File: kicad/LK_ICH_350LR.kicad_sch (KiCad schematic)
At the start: 27 parts, among them Q1 BTA12-700SW, U2 PC123

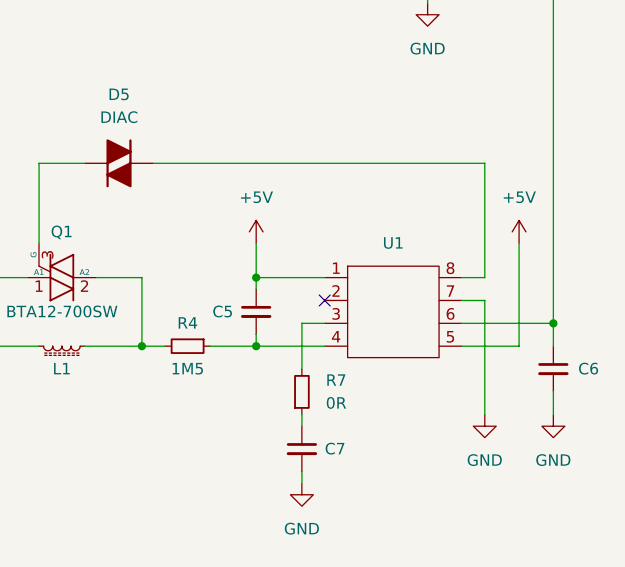
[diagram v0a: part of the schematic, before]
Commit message: update dimmer control ic symbol
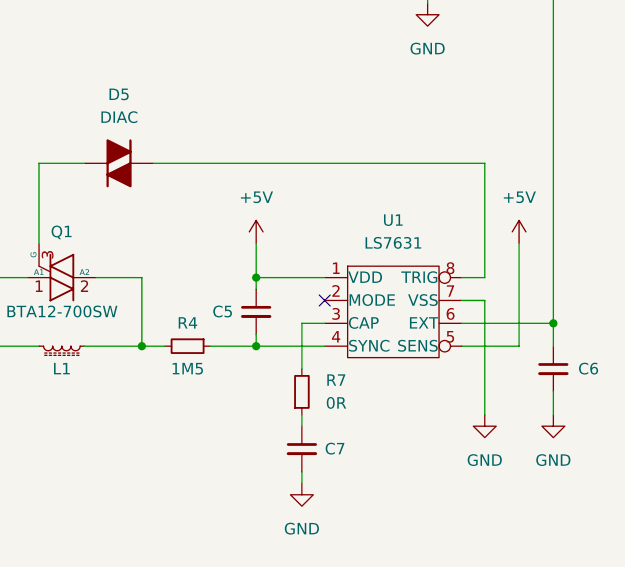
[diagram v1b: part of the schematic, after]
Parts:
- U1: value ~ -> LS7631; footprint (none) -> Package_SO:SOIC-8_3.9x4.9mm_P1.27mm; symbol LK913A4:DIM -> LK913A4:LS7631
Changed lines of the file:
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@@
     )
   )
-  (symbol (lib_id "LK913A4:DIM") (at 135.89 106.68 0) (unit 1)
+  (symbol (lib_id "LK913A4:LS7631") (at 135.89 106.68 0) (unit 1)
     (in_bom yes) (on_board yes) (dnp no) (fields_autoplaced)
-    (property "Reference" "U1" (at 135.89 99.06 0)
+    (property "Reference" "U1" (at 135.89 96.52 0)
       (effects (font (size 1.27 1.27)))
     )
-    (property "Value" "~" (at 135.89 106.68 0)
+    (property "Value" "LS7631" (at 135.89 99.06 0)
       (effects (font (size 1.27 1.27)))
     )
-    (property "Footprint" "" (at 135.89 106.68 0)
+    (property "Footprint" "Package_SO:SOIC-8_3.9x4.9mm_P1.27mm" (at 135.89 106.68 0)
       (effects (font (size 1.27 1.27)) hide)
     )
-    (property "Datasheet" "" (at 135.89 106.68 0)
+    (property "Datasheet" "http://www.lsicsi.com/pdfs/Data_Sheets/LS7631_LS7632.pdf" (at 135.89 106.68 0)
       (effects (font (size 1.27 1.27)) hide)
     )

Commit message: add note about diac
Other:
- note added: "This may not actually be a diac, but could be a small signal diode per the SLB0587 reference schematic."
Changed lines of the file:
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@@
   (title_block
     (title "LK ICH Dimmer 350 LR")
-    (date "2023-12-04")
-    (rev "1")
+    (date "2023-12-09")
+    (rev "2")
     (comment 1 "LK913CB4")
     (comment 2 "LK913A4")
@@
     (effects (font (size 1.27 1.27)) (justify left bottom))
   )
+  (text "This may not actually be a diac,\nbut could be a small signal diode\nper the SLB0587 reference schematic."
+    (at 64.77 86.36 0)
+    (effects (font (size 1.27 1.27)) (justify left bottom))
+  )

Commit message: fix capacitance of c3
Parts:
- C3: value 22u -> 100u
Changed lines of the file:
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@@
   (title_block
     (title "LK ICH Dimmer 350 LR")
-    (date "2023-12-09")
-    (rev "2")
+    (date "2023-12-17")
+    (rev "3")
     (comment 1 "LK913CB4")
     (comment 2 "LK913A4")
@@
       (effects (font (size 1.27 1.27)) (justify left))
     )
-    (property "Value" "22u" (at 128.27 171.45 0)
-      (effects (font (size 1.27 1.27)))
-    )
+    (property "Value" "100u" (at 128.27 171.45 0)
+      (effects (font (size 1.27 1.27)))
+    )

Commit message: fix annotations
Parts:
- renumbered C2 to C1, D3 to CR1, R5 to R2, R7 to R3, R1 to R5, R3 to R7, R2 to R8, D4 to VR1
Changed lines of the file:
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@@
   (symbol (lib_id "Device:R_Small") (at 153.67 68.58 180) (unit 1)
     (in_bom yes) (on_board yes) (dnp no) (fields_autoplaced)
-    (property "Reference" "R1" (at 156.21 67.31 0)
+    (property "Reference" "R5" (at 156.21 67.31 0)
       (effects (font (size 1.27 1.27)) (justify right))
     )
@@
       (project "LK_ICH_350LR"
         (path "/00661e67-d895-4a4d-8f6d-597ae5750c96"
-          (reference "R1") (unit 1)
+          (reference "R5") (unit 1)
         )
       )
@@
   (symbol (lib_id "Device:R_Small") (at 96.52 62.23 90) (mirror x) (unit 1)
     (in_bom yes) (on_board yes) (dnp no)
-    (property "Reference" "R3" (at 96.52 64.77 90)
+    (property "Reference" "R7" (at 96.52 64.77 90)
       (effects (font (size 1.27 1.27)))
     )
@@
       (project "LK_ICH_350LR"
         (path "/00661e67-d895-4a4d-8f6d-597ae5750c96"
-          (reference "R3") (unit 1)
+          (reference "R7") (unit 1)
         )
       )
@@
   (symbol (lib_id "Device:D_Zener_Small") (at 107.95 165.1 90) (mirror x) (unit 1)
     (in_bom yes) (on_board yes) (dnp no)
-    (property "Reference" "D4" (at 107.95 158.75 90)
+    (property "Reference" "VR1" (at 107.95 158.75 90)
       (effects (font (size 1.27 1.27)))
     )
@@
       (project "LK_ICH_350LR"
         (path "/00661e67-d895-4a4d-8f6d-597ae5750c96"
-          (reference "D4") (unit 1)
+          (reference "VR1") (unit 1)
         )
       )
@@
   (symbol (lib_id "Device:D_Small") (at 114.3 168.91 0) (mirror x) (unit 1)
     (in_bom yes) (on_board yes) (dnp no)
-    (property "Reference" "D3" (at 114.3 166.37 0)
+    (property "Reference" "CR1" (at 114.3 166.37 0)
       (effects (font (size 1.27 1.27)))
     )
@@
       (project "LK_ICH_350LR"
         (path "/00661e67-d895-4a4d-8f6d-597ae5750c96"
-          (reference "D3") (unit 1)
+          (reference "CR1") (unit 1)
         )
       )
@@
   (symbol (lib_id "Device:R_Small") (at 125.73 115.57 0) (mirror x) (unit 1)
     (in_bom yes) (on_board yes) (dnp no)
-    (property "Reference" "R7" (at 129.54 114.3 0)
+    (property "Reference" "R3" (at 129.54 114.3 0)
       (effects (font (size 1.27 1.27)))
     )
@@
       (project "LK_ICH_350LR"
         (path "/00661e67-d895-4a4d-8f6d-597ae5750c96"
-          (reference "R7") (unit 1)
+          (reference "R3") (unit 1)
         )
       )
@@
   (symbol (lib_id "Device:R_Small") (at 96.52 57.15 90) (unit 1)
     (in_bom yes) (on_board yes) (dnp no)
-    (property "Reference" "R2" (at 96.52 52.07 90)
+    (property "Reference" "R8" (at 96.52 52.07 90)
       (effects (font (size 1.27 1.27)))
     )
@@
       (project "LK_ICH_350LR"
         (path "/00661e67-d895-4a4d-8f6d-597ae5750c96"
-          (reference "R2") (unit 1)
+          (reference "R8") (unit 1)
         )
       )
@@
   (symbol (lib_id "Device:R_Small") (at 120.65 168.91 90) (mirror x) (unit 1)
     (in_bom yes) (on_board yes) (dnp no)
-    (property "Reference" "R5" (at 120.65 166.37 90)
+    (property "Reference" "R2" (at 120.65 166.37 90)
       (effects (font (size 1.27 1.27)))
     )
@@
       (project "LK_ICH_350LR"
         (path "/00661e67-d895-4a4d-8f6d-597ae5750c96"
-          (reference "R5") (unit 1)
+          (reference "R2") (unit 1)
         )
       )
@@
   (symbol (lib_id "Device:C_Small") (at 85.09 106.68 0) (unit 1)
     (in_bom yes) (on_board yes) (dnp no)
-    (property "Reference" "C2" (at 83.82 100.33 0)
+    (property "Reference" "C1" (at 83.82 100.33 0)
       (effects (font (size 1.27 1.27)) (justify left))
     )
@@
       (project "LK_ICH_350LR"
         (path "/00661e67-d895-4a4d-8f6d-597ae5750c96"
-          (reference "C2") (unit 1)
-        )
-      )
+          (reference "C1") (unit 1)
+        )
+      )

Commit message: add note about fuse holder and terminal block parts
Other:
- note added: "F1 fuse holder: Schurter FAC 5x20mm, slotted cap J1/J2 terminal block: P6.35mm"
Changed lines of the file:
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@@
   (title_block
     (title "LK ICH Dimmer 350 LR")
-    (date "2023-12-17")
-    (rev "3")
+    (date "2023-12-18")
+    (rev "4")
     (comment 1 "LK913CB4")
     (comment 2 "LK913A4")
@@
     (effects (font (size 1.27 1.27)) (justify left bottom))
   )
+  (text "F1 fuse holder: Schurter FAC 5x20mm, slotted cap\nJ1/J2 terminal block: P6.35mm"
+    (at 227.33 153.67 0)
+    (effects (font (size 1.27 1.27)) (justify left bottom))
+  )
